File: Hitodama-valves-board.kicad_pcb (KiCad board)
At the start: 2 copper layers, 66 x 64.8 mm, 32 parts, among them J1 Solenoid A, J10 PWMB, J11 STANDBY, J2 Solenoid B, J3 Pressure_amp_b, J4 Pressure_amp_a, J5 PWMA, J6 AIN2, J7 AIN1, J8 BIN1, J9 BIN2, U1 LM358, U2 Pressure_b, U3 Pressure_a, U5 Pololu-713

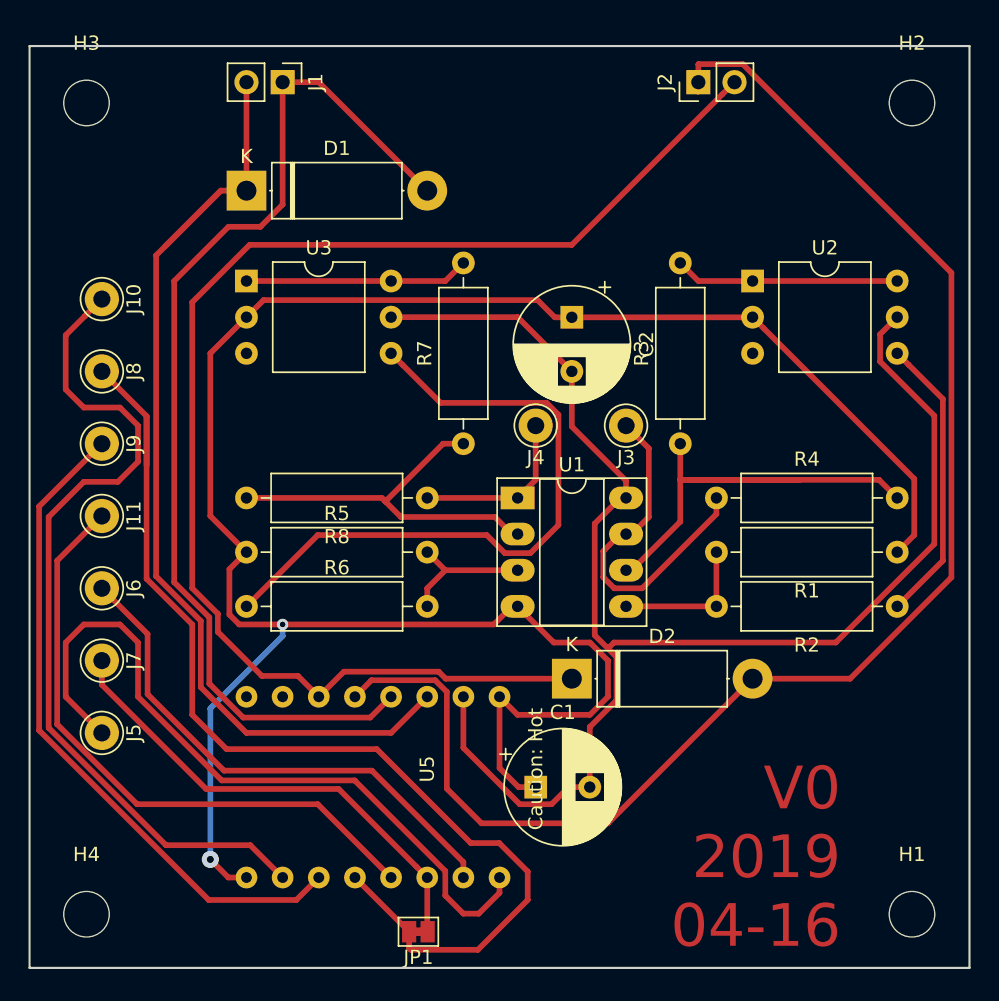
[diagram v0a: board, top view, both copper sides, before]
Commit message: fixed capacitor colliding motor driver board
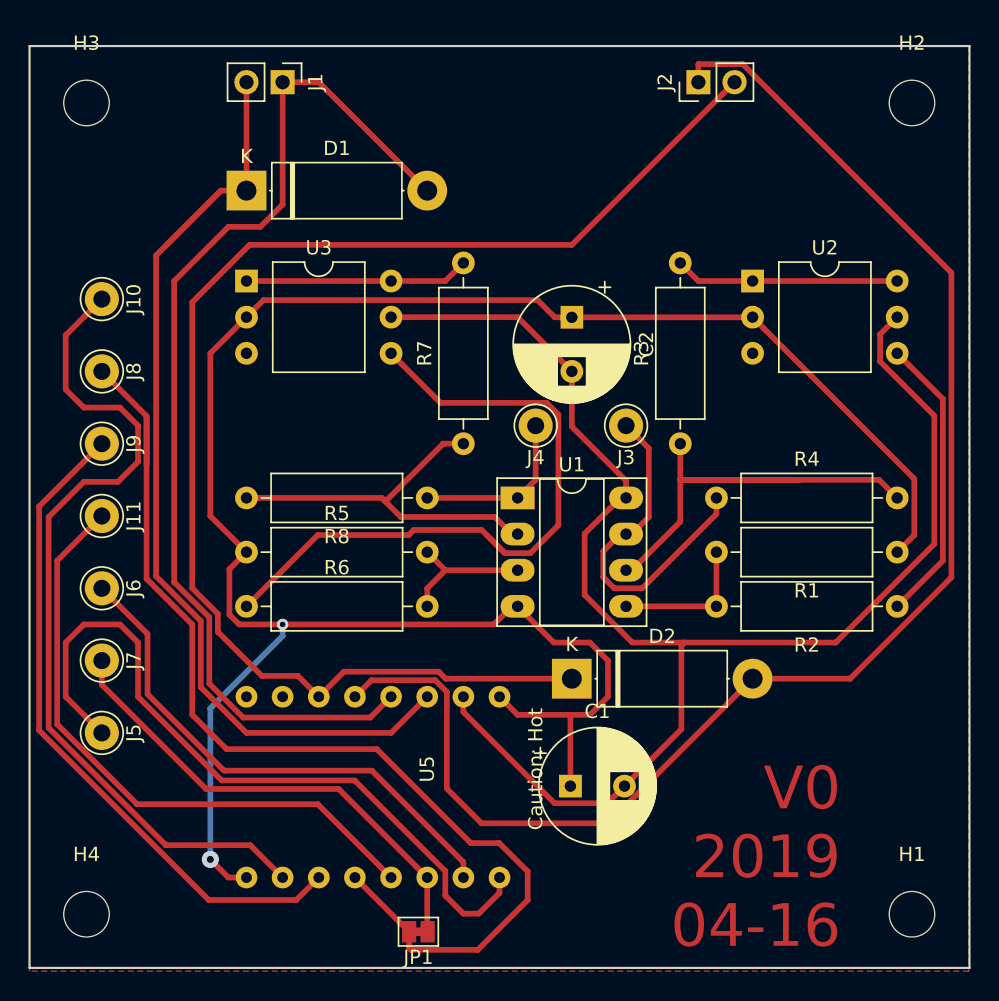
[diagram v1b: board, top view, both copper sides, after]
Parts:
- moved C1 2.44 mm to (38.0, 52.0)
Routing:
- net GND: track 151.8 -> 148.7 mm
- net Net-(R6-Pad1): track 46.6 -> 48.7 mm
- net VCC: track 106.2 -> 107.2 mm
- added copper zone on F.Cu, net GND
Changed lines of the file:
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@@
     (thickness 1.6)
     (drawings 5)
-    (tracks 236)
+    (tracks 237)
     (zones 0)
     (modules 32)
@@
   )
   (module Capacitor_THT:CP_Radial_D8.0mm_P3.80mm (layer F.Cu)
-    (at 35.56 52.07)
+    (at 38 52)
     (descr "CP, Radial series, Radial, pin pitch=3.80mm, , diameter=8mm, Electrolytic Capacitor")
     (tags "CP Radial series Radial pin pitch 3.80mm  diameter 8mm Electrolytic Capacitor")
@@
   (segment (start 34.29 19.05) (end 38.1 22.86) (width 0.4) (layer F.Cu) (net 1) (status 20))
   (segment (start 25.4 19.05) (end 34.29 19.05) (width 0.4) (layer F.Cu) (net 1) (status 10))
-  (segment (start 34.439999 53.270001) (end 30.48 49.310002) (width 0.4) (layer F.Cu) (net 1))
-  (segment (start 30.48 49.310002) (end 30.48 45.72) (width 0.4) (layer F.Cu) (net 1) (status 20))
-  (segment (start 36.680001 53.270001) (end 34.439999 53.270001) (width 0.4) (layer F.Cu) (net 1))
-  (segment (start 37.880002 52.07) (end 36.680001 53.270001) (width 0.4) (layer F.Cu) (net 1))
-  (segment (start 37.880002 52.07) (end 39.36 52.07) (width 0.4) (layer F.Cu) (net 1) (status 20))
-  (segment (start 41.51 31.75) (end 39.709979 33.550021) (width 0.4) (layer F.Cu) (net 1) (status 10))
-  (segment (start 41.91 31.75) (end 41.51 31.75) (width 0.4) (layer F.Cu) (net 1) (status 30))
-  (segment (start 39.709979 33.550021) (end 39.709979 41.401436) (width 0.4) (layer F.Cu) (net 1))
-  (segment (start 41.240011 42.931468) (end 41.240011 45.968532) (width 0.4) (layer F.Cu) (net 1))
-  (segment (start 39.36 47.848543) (end 41.240011 45.968532) (width 0.4) (layer F.Cu) (net 1))
-  (segment (start 39.36 52.07) (end 39.36 47.848543) (width 0.4) (layer F.Cu) (net 1) (status 10))
   (segment (start 38.1 26.74) (end 38.1 22.86) (width 0.4) (layer F.Cu) (net 1) (status 20))
   (segment (start 41.91 30.55) (end 38.1 26.74) (width 0.4) (layer F.Cu) (net 1))
   (segment (start 41.91 31.75) (end 41.91 30.55) (width 0.4) (layer F.Cu) (net 1) (status 10))
-  (segment (start 39.709979 41.401436) (end 40.64 42.331457) (width 0.4) (layer F.Cu) (net 1))
-  (segment (start 40.64 42.331457) (end 41.240011 42.931468) (width 0.4) (layer F.Cu) (net 1))
   (segment (start 59.759999 20.250001) (end 59.759999 22.166001) (width 0.4) (layer F.Cu) (net 1))
-  (segment (start 56.643998 41.91) (end 41.061457 41.91) (width 0.4) (layer F.Cu) (net 1))
   (segment (start 60.96 19.05) (end 59.759999 20.250001) (width 0.4) (layer F.Cu) (net 1) (status 10))
-  (segment (start 41.061457 41.91) (end 40.64 42.331457) (width 0.4) (layer F.Cu) (net 1))
   (segment (start 63.569978 25.97598) (end 63.569978 34.98402) (width 0.4) (layer F.Cu) (net 1))
   (segment (start 59.759999 22.166001) (end 63.569978 25.97598) (width 0.4) (layer F.Cu) (net 1))
   (segment (start 63.569978 34.98402) (end 56.643998 41.91) (width 0.4) (layer F.Cu) (net 1))
+  (segment (start 41.000001 52.799999) (end 41.8 52) (width 0.4) (layer F.Cu) (net 1))
+  (segment (start 40.599999 53.200001) (end 41.000001 52.799999) (width 0.4) (layer F.Cu) (net 1))
+  (segment (start 36.882371 53.200001) (end 40.599999 53.200001) (width 0.4) (layer F.Cu) (net 1))
+  (segment (start 30.48 46.79763) (end 36.882371 53.200001) (width 0.4) (layer F.Cu) (net 1))
+  (segment (start 30.48 45.72) (end 30.48 46.79763) (width 0.4) (layer F.Cu) (net 1))
+  (segment (start 42.35293 41.91) (end 39 38.55707) (width 0.4) (layer F.Cu) (net 1))
+  (segment (start 41.51 31.75) (end 41.91 31.75) (width 0.4) (layer F.Cu) (net 1))
+  (segment (start 39 34.26) (end 41.51 31.75) (width 0.4) (layer F.Cu) (net 1))
+  (segment (start 39 38.55707) (end 39 34.26) (width 0.4) (layer F.Cu) (net 1))
+  (segment (start 41.8 52) (end 45.8 48) (width 0.4) (layer F.Cu) (net 1))
+  (segment (start 45.8 42.11) (end 46 41.91) (width 0.4) (layer F.Cu) (net 1))
+  (segment (start 45.8 48) (end 45.8 42.11) (width 0.4) (layer F.Cu) (net 1))
+  (segment (start 56.643998 41.91) (end 46 41.91) (width 0.4) (layer F.Cu) (net 1))
+  (segment (start 46 41.91) (end 42.35293 41.91) (width 0.4) (layer F.Cu) (net 1))
   (segment (start 50.79 19.06) (end 50.8 19.05) (width 0.4) (layer F.Cu) (net 2) (status 30))
   (segment (start 38.1 19.06) (end 50.79 19.06) (width 0.4) (layer F.Cu) (net 2) (status 30))
-  (segment (start 34.36 52.07) (end 35.56 52.07) (width 0.4) (layer F.Cu) (net 2) (status 20))
-  (segment (start 33.02 50.73) (end 34.36 52.07) (width 0.4) (layer F.Cu) (net 2))
-  (segment (start 33.02 45.72) (end 33.02 50.73) (width 0.4) (layer F.Cu) (net 2) (status 10))
   (segment (start 15.24 19.05) (end 12.7 21.59) (width 0.4) (layer F.Cu) (net 2) (status 10))
   (segment (start 12.7 33.02) (end 15.24 35.56) (width 0.4) (layer F.Cu) (net 2) (status 20))
   (segment (start 12.7 21.59) (end 12.7 33.02) (width 0.4) (layer F.Cu) (net 2))
   (segment (start 33.02 45.72) (end 34.29 46.99) (width 0.4) (layer F.Cu) (net 2) (status 10))
-  (segment (start 34.29 46.99) (end 39.37 46.99) (width 0.4) (layer F.Cu) (net 2))
   (segment (start 39.37 46.99) (end 40.64 45.72) (width 0.4) (layer F.Cu) (net 2))
   (segment (start 40.64 45.72) (end 40.64 43.18) (width 0.4) (layer F.Cu) (net 2))
@@
   (segment (start 35.689999 17.849999) (end 36.9 19.06) (width 0.4) (layer F.Cu) (net 2))
   (segment (start 15.24 19.05) (end 16.440001 17.849999) (width 0.4) (layer F.Cu) (net 2) (status 10))
+  (segment (start 38 52) (end 38 46.99) (width 0.4) (layer F.Cu) (net 2))
+  (segment (start 34.29 46.99) (end 38 46.99) (width 0.4) (layer F.Cu) (net 2))
+  (segment (start 38 46.99) (end 39.37 46.99) (width 0.4) (layer F.Cu) (net 2))
   (segment (start 15.24 2.54) (end 15.24 10.16) (width 0.4) (layer F.Cu) (net 3) (status 30))
   (segment (start 13.44 10.16) (end 9.559989 14.040011) (width 0.4) (layer F.Cu) (net 3))
@@
   (segment (start 27.94 38.1) (end 29.21 36.83) (width 0.4) (layer F.Cu) (net 11))
   (segment (start 27.94 39.37) (end 27.94 38.1) (width 0.4) (layer F.Cu) (net 11) (status 10))
-  (segment (start 20.250001 34.359999) (end 32.122949 34.359999) (width 0.4) (layer F.Cu) (net 12))
   (segment (start 32.122949 34.359999) (end 33.39294 35.62999) (width 0.4) (layer F.Cu) (net 12))
   (segment (start 33.39294 35.62999) (end 35.18706 35.62999) (width 0.4) (layer F.Cu) (net 12))
@@
   (segment (start 26.199999 22.389999) (end 25.4 21.59) (width 0.4) (layer F.Cu) (net 12) (status 30))
   (segment (start 15.24 39.37) (end 20.250001 34.359999) (width 0.4) (layer F.Cu) (net 12) (status 10))
+  (segment (start 20.250001 34.359999) (end 26.640001 34.359999) (width 0.4) (layer F.Cu) (net 12))
+  (segment (start 26.640001 34.359999) (end 27 34) (width 0.4) (layer F.Cu) (net 12))
+  (segment (start 31.76295 34) (end 33.39294 35.62999) (width 0.4) (layer F.Cu) (net 12))
+  (segment (start 27 34) (end 31.76295 34) (width 0.4) (layer F.Cu) (net 12))
   (segment (start 34.29 34.29) (end 34.69 34.29) (width 0.4) (layer F.Cu) (net 13) (status 30))
   (segment (start 33.89 34.29) (end 34.29 34.29) (width 0.4) (layer F.Cu) (net 13))
@@
   (segment (start 17.78 58.42) (end 15.509999 56.149999) (width 0.4) (layer F.Cu) (net 27))
   (segment (start 3.880001 18.979999) (end 5.08 17.78) (width 0.4) (layer F.Cu) (net 27))
+  (zone (net 2) (net_name GND) (layer F.Cu) (hatch edge 0.508)
+    (connect_pads (clearance 0.508))
+    (min_thickness 0.254)
+    (fill yes (arc_segments 16) (thermal_gap 0.508) (thermal_bridge_width 0.508))
+    (polygon
+      (pts
+        (xy 0 0) (xy 66 0) (xy 66 65) (xy 0 65)
+      )
+    )
+  )
 )

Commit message: improved adding +12v connector
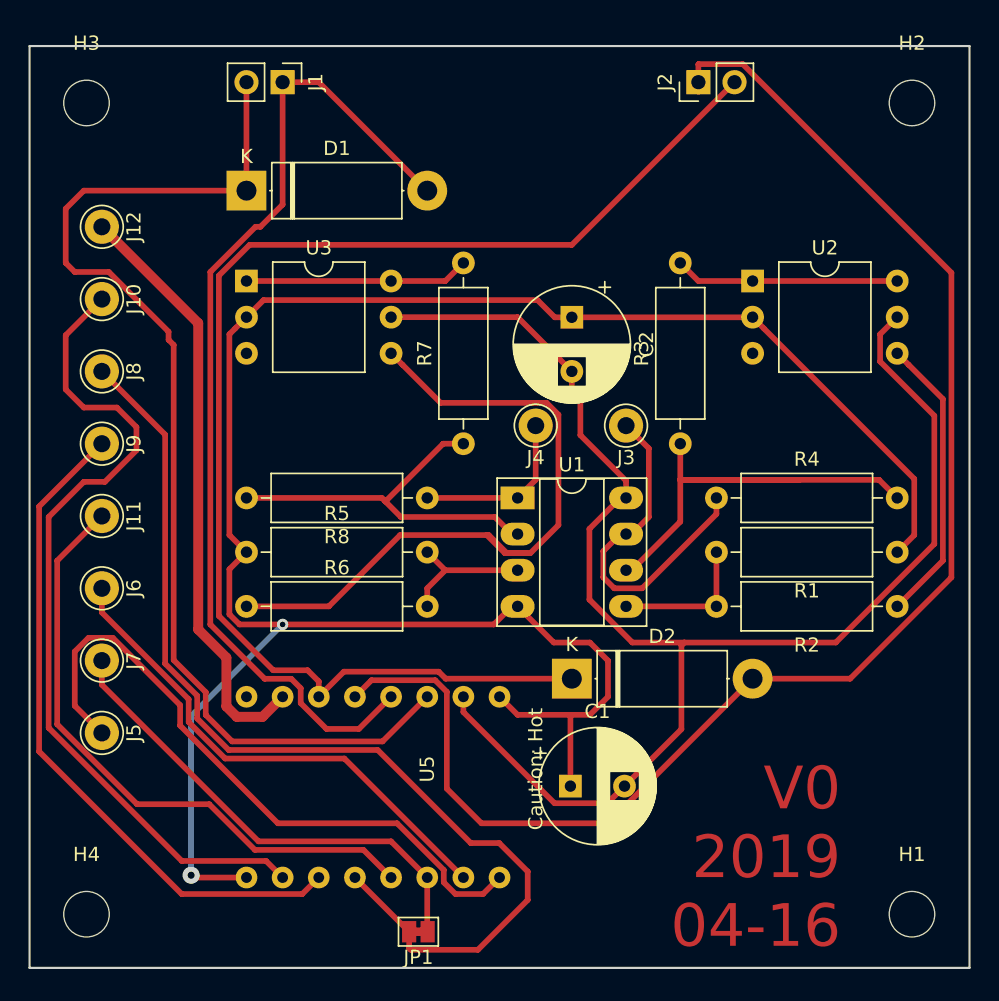
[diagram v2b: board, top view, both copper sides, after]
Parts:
- added J12: +12v_SUPPLY, Connector_Pin:Pin_D1.0mm_L10.0mm_LooseFit, F.Cu at (5.08, 12.7)
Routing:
- net +12V: track 0.00 -> 42.2 mm
- net Net-(D1-Pad1): track 71.3 -> 79.5 mm
- net Net-(J5-Pad1): track 51.7 -> 46.0 mm
- net Net-(D1-Pad2): track 75.4 -> 71.0 mm
- net Net-(J8-Pad1): track 76.7 -> 73.2 mm
- net Net-(D2-Pad1): track 96.1 -> 94.5 mm
- net GND: track 148.7 -> 150.1 mm
- net Net-(R6-Pad1): track 48.7 -> 50.0 mm
- net Net-(J6-Pad1): track 36.9 -> 35.7 mm
- net Net-(J10-Pad1): track 59.6 -> 58.8 mm
- net Net-(J9-Pad1): track 47.2 -> 47.7 mm
- removed copper zone on F.Cu, net GND
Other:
- net class powers: clearance 0.5 -> 0.3

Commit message: Change track definitions to fit Fablab's
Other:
- net class Default: clearance 0.2 -> 0.3; via_dia 1.2 -> 1.4; via_drill 0.5 -> 0.8
- net class powers: via_dia 0.8 -> 1.4; via_drill 0.4 -> 0.8
- rule trace_clearance: 0.2 -> 0.3
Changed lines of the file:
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@@
-(kicad_pcb (version 20171130) (host pcbnew "(5.0.1)-4")
+(kicad_pcb (version 20171130) (host pcbnew 5.1.1-8be2ce7~80~ubuntu18.04.1)
   (general
     (thickness 1.6)
@@
   (setup
     (last_trace_width 0.4)
-    (trace_clearance 0.2)
+    (trace_clearance 0.3)
     (zone_clearance 0.508)
     (zone_45_only no)
     (trace_min 0.2)
-    (segment_width 0.2)
-    (edge_width 0.15)
-    (via_size 1.2)
-    (via_drill 0.5)
+    (via_size 1.4)
+    (via_drill 0.8)
     (via_min_size 0.4)
     (via_min_drill 0.3)
@@
     (uvia_min_size 0.2)
     (uvia_min_drill 0.1)
+    (edge_width 0.15)
+    (segment_width 0.2)
     (pcb_text_width 0.3)
     (pcb_text_size 1.5 1.5)
@@
   (net 27 "Net-(J10-Pad1)")
   (net_class Default "This is the default net class."
-    (clearance 0.2)
+    (clearance 0.3)
     (trace_width 0.4)
-    (via_dia 1.2)
-    (via_drill 0.5)
+    (via_dia 1.4)
+    (via_drill 0.8)
     (uvia_dia 0.3)
     (uvia_drill 0.1)
+    (diff_pair_width 0.3)
+    (diff_pair_gap 0.3)
     (add_net /stby)
     (add_net GND)
@@
     (clearance 0.3)
     (trace_width 0.7)
-    (via_dia 0.8)
-    (via_drill 0.4)
+    (via_dia 1.4)
+    (via_drill 0.8)
     (uvia_dia 0.3)
     (uvia_drill 0.1)
+    (diff_pair_width 0.3)
+    (diff_pair_gap 0.3)
     (add_net +12V)
   )

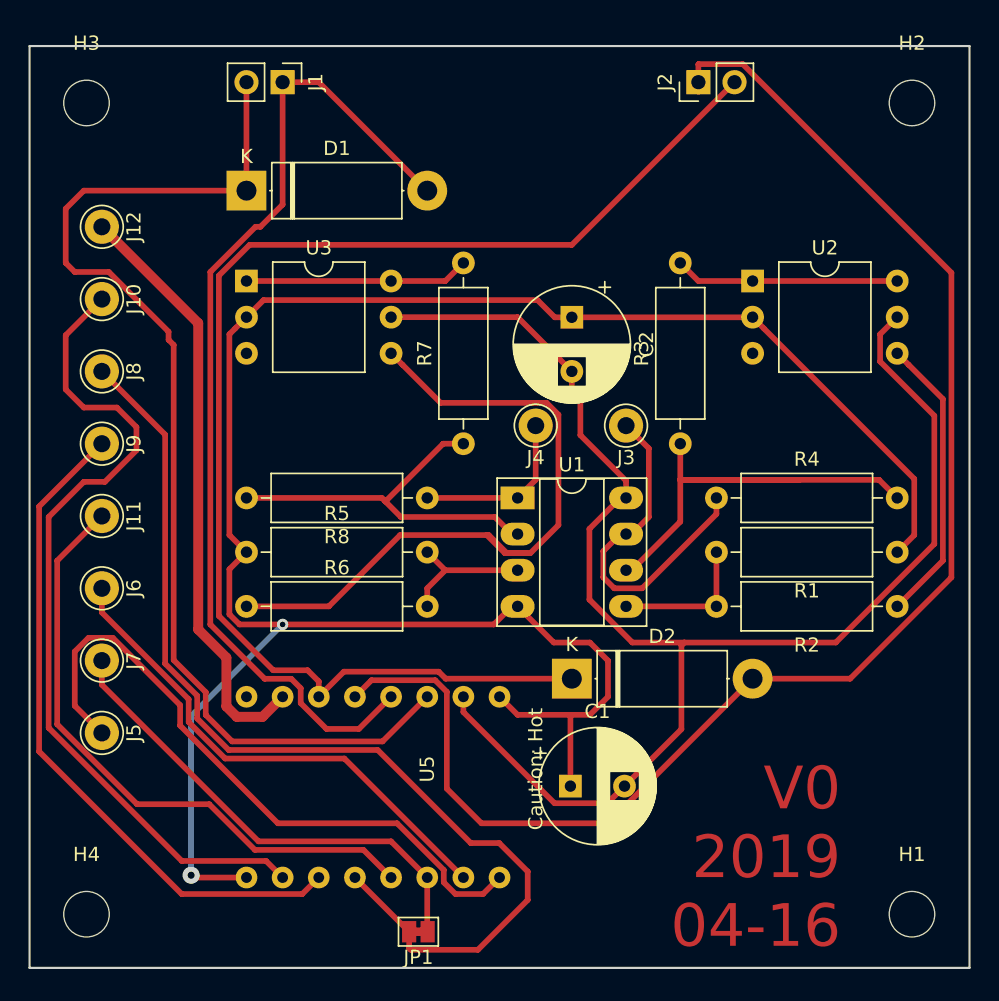
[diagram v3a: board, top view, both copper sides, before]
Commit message: changed design rules for milling machine and consequently re-routed everyhting
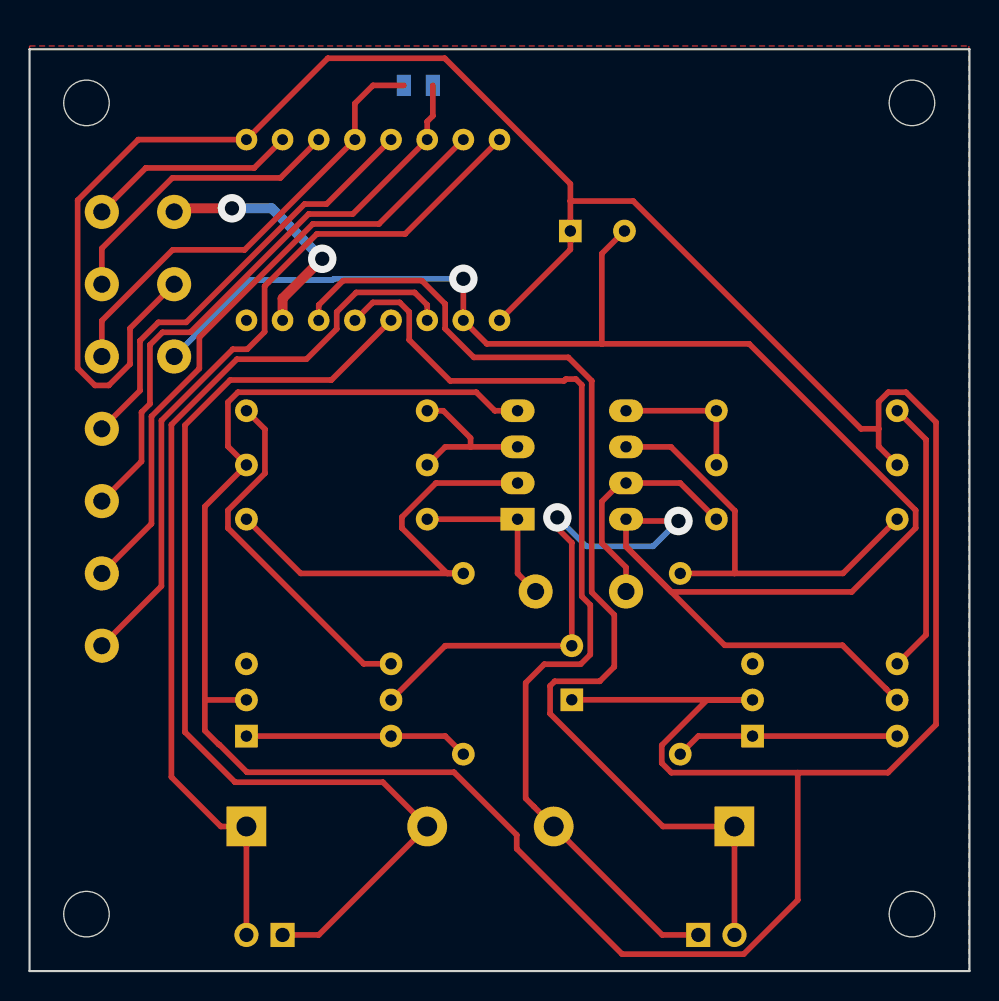
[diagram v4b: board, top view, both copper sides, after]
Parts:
- added J13: VCC supply, Connector_Pin:Pin_D1.0mm_L10.0mm_LooseFit, B.Cu at (10.2, 21.8)
- added J14: GND, Connector_Pin:Pin_D1.0mm_L10.0mm_LooseFit, B.Cu at (10.2, 16.7)
- C1, C2, D1, D2, H1, H2, H3, H4, J1, J10, J11, J12, J2, J3, J4, J5, J6, J7, J8, J9, R1, R2, R3, R4, R5, R6, R7, R8, U1, U2, U3, U5: moved to B.Cu
- JP1: footprint Jumper:SolderJumper-2_P1.3mm_Bridged_Pad1.0x1.5mm -> Jumper:SolderJumper-2_P1.3mm_Bridged2Bar_Pad1.0x1.5mm; moved to B.Cu
- moved J1 59.9 mm to (17.8, 62.5), turned to 90 degrees
- moved J2 59.9 mm to (47.0, 62.5), turned to 270 degrees
- moved JP1 59.5 mm to (27.3, 2.76)
- moved H1 57.0 mm to (62.0, 3.99)
- moved H4 57.0 mm to (4.00, 3.99)
- moved H2 57.0 mm to (62.0, 61.0)
- moved H3 57.0 mm to (4.00, 61.0)
- moved D1 44.7 mm to (15.2, 54.8)
- moved C1 39.0 mm to (38.0, 13.0)
- moved U2 32.0 mm to (50.8, 48.5)
- moved U3 32.0 mm to (15.2, 48.5)
- moved C2 26.9 mm to (38.1, 45.9), turned to 90 degrees
- moved U5 26.4 mm to (33.0, 19.3), turned to 90 degrees
- moved D2 15.4 mm to (49.5, 54.8), turned to 180 degrees
- moved R2 13.7 mm to (61.0, 25.6)
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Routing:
- net GND: track 150.1 -> 288.0 mm, vias 2 -> 0
- net VCC: track 106.9 -> 159.2 mm, vias 0 -> 3
- net Net-(J10-Pad1): track 58.8 -> 14.8 mm
- net Net-(J8-Pad1): track 73.2 -> 32.1 mm
- net Net-(D2-Pad2): track 104.9 -> 68.9 mm
- net Net-(J9-Pad1): track 47.7 -> 20.9 mm
- net +12V: track 42.2 -> 17.5 mm, vias 0 -> 2
- net Net-(R6-Pad1): track 50.0 -> 25.3 mm
- net Net-(D2-Pad1): track 94.5 -> 76.5 mm
- net Net-(D1-Pad1): track 79.5 -> 63.1 mm
- net /stby: track 43.9 -> 30.8 mm
- net Net-(J3-Pad1): track 24.7 -> 16.7 mm
- net Net-(J6-Pad1): track 35.7 -> 43.7 mm
- net Net-(J7-Pad1): track 34.0 -> 41.8 mm
- net Net-(J5-Pad1): track 46.0 -> 51.4 mm
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- added copper zone on F.Cu, net GND
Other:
- net class Default: via_dia 1.4 -> 2; via_drill 0.8 -> 1
- net class powers: via_dia 1.4 -> 2; via_drill 0.8 -> 1
- board text removed: "V0 2019 04-16"
